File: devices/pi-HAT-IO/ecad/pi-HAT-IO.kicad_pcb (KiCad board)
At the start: 4 copper layers, 65 x 56 mm, 57 parts, among them J1 GPIO, J10 JST XH, J2 Mini-Fit Jr, J3 JST SH, J4 JST SH, J5 JST SH, J6 PC FAN HEADER, J7 PC FAN HEADER, J8 JST PH, J9 JST PH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

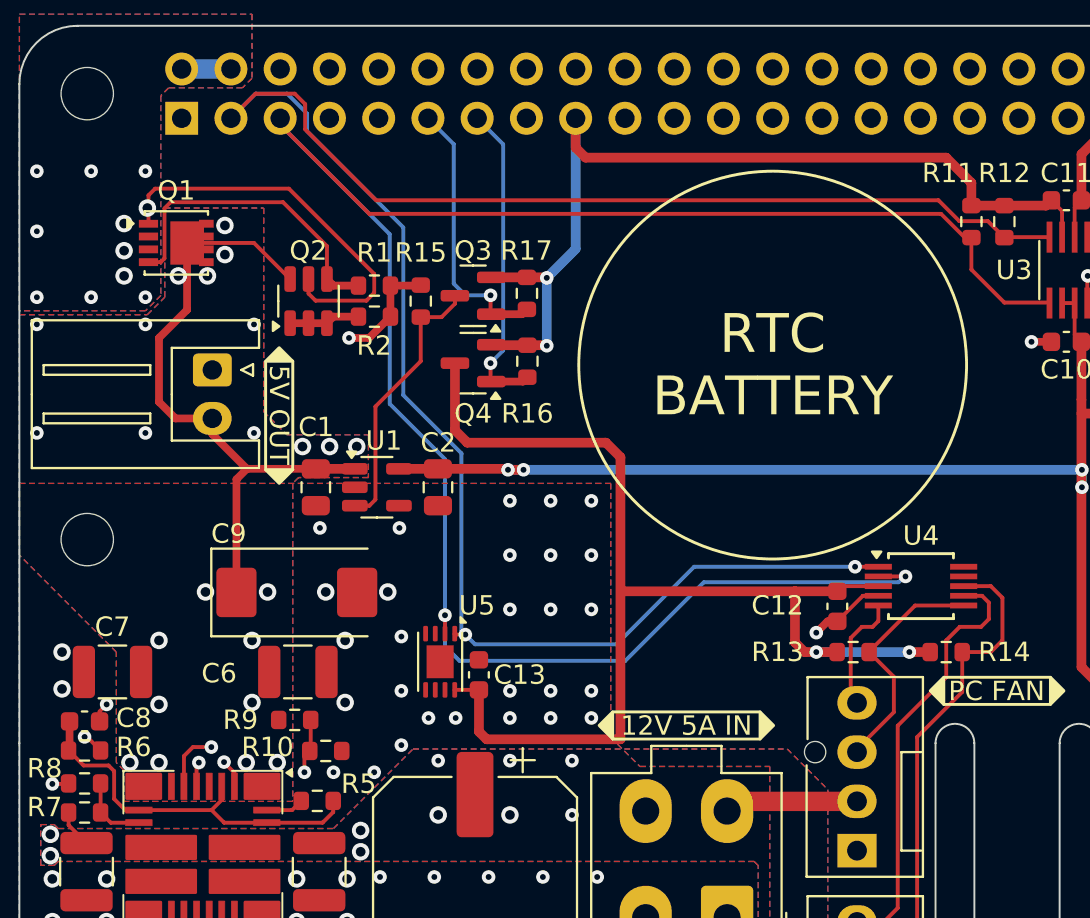
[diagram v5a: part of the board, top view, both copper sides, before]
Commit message: Small Correction for pi-HAT
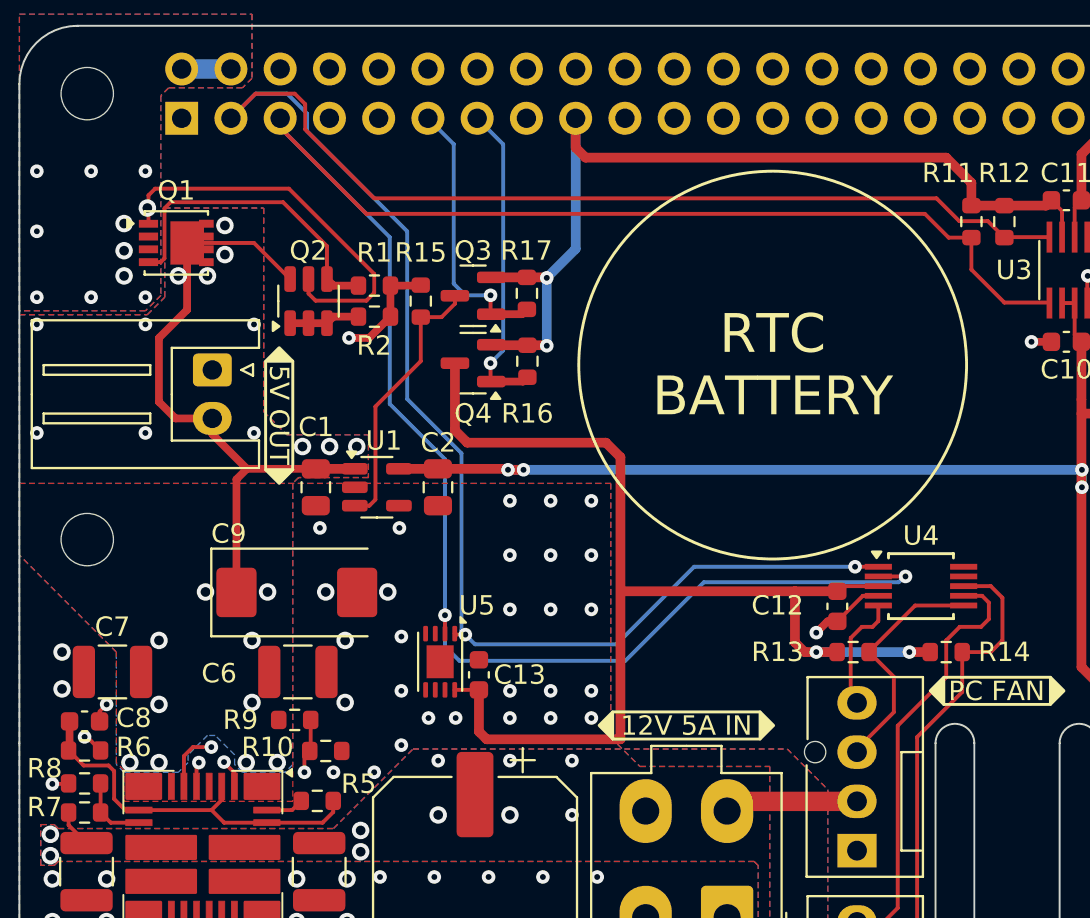
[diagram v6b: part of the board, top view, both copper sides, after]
